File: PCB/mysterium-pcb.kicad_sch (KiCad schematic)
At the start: 221 parts, among them J1 AVR-ISP-6, J2 OLED, J3 TRRS1, J4 TRRS2, SW0 KEYSW, SW1 KEYSW, SW10 KEYSW, SW100 KEYSW, SW101 KEYSW, SW102 KEYSW, SW103 Rotary_Encoder_Switch, SW11 KEYSW, SW12 KEYSW, SW13 KEYSW, SW14 KEYSW, SW15 KEYSW, SW16 KEYSW, SW17 KEYSW, SW18 KEYSW, SW19 KEYSW, SW2 KEYSW, SW20 KEYSW, SW21 KEYSW, SW22 KEYSW, SW23 KEYSW, SW24 KEYSW, SW25 KEYSW, SW26 KEYSW, SW27 KEYSW, SW28 KEYSW, SW29 KEYSW, SW3 KEYSW, SW30 KEYSW, SW31 KEYSW, SW32 KEYSW, SW33 KEYSW, SW34 KEYSW, SW35 KEYSW, SW36 KEYSW, SW37 KEYSW, SW38 KEYSW, SW39 KEYSW, SW4 KEYSW, SW40 KEYSW, SW41 KEYSW, SW42 KEYSW, SW43 KEYSW, SW44 KEYSW, SW45 KEYSW, SW46 KEYSW, SW47 KEYSW, SW48 KEYSW, SW49 KEYSW, SW5 KEYSW, SW50 KEYSW, SW51 KEYSW, SW52 KEYSW, SW53 KEYSW, SW54 KEYSW, SW55 KEYSW, SW56 KEYSW, SW57 KEYSW, SW58 KEYSW, SW59 KEYSW, SW6 KEYSW, SW60 KEYSW, SW61 KEYSW, SW62 KEYSW, SW63 KEYSW, SW64 KEYSW, SW65 KEYSW, SW66 KEYSW, SW67 KEYSW, SW68 KEYSW, SW69 KEYSW, SW7 KEYSW, SW70 KEYSW, SW71 KEYSW, SW72 KEYSW, SW73 KEYSW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

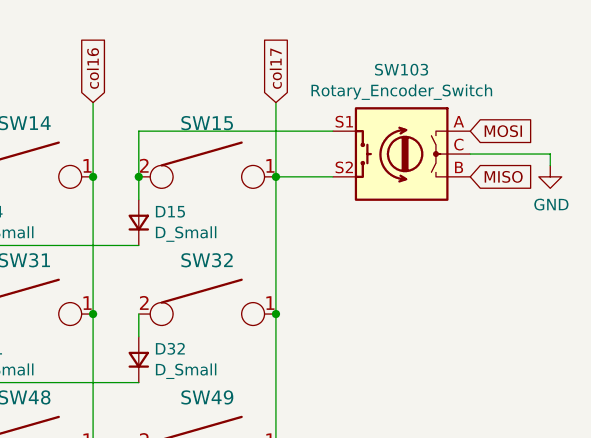
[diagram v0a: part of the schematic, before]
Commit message: Modifying PCB with hotswap keys
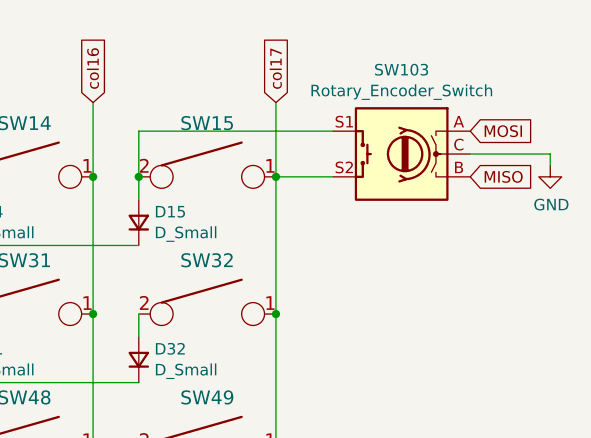
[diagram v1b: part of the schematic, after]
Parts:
- J3, J4: footprint kbd:MJ-4PP-9_1side -> My footprints:MJ-4PP-9_1side
- SW0, SW1, SW10, SW100, SW102, SW11, SW12, SW13, SW14, SW15, SW16, SW17, SW18, SW19, SW2, SW20, SW21, SW22, SW23, SW24, SW25, SW26, SW27, SW28, SW3, SW30, SW31, SW32, SW34, SW35, SW36, SW37, SW38, SW39, SW4, SW40, SW41, SW42, SW43, SW44, SW45, SW47, SW48, SW49, SW5, SW52, SW53, SW54, SW55, SW56, SW57, SW58, SW59, SW6, SW60, SW61, SW62, SW65, SW66, SW67, SW68, SW69, SW7, SW70, SW71, SW72, SW73, SW74, SW76, SW8, SW80, SW83, SW84, SW89, SW9, SW92, SW93, SW94, SW96, SW98, SW99: footprint cftkb:SW_Cherry_MX1A_1.00u_PCB-NOSCREEN -> acheron_MXH_MetalRings:MX100H
- SW101, SW50: footprint cftkb:SW_Cherry_MX1A_1.75u_PCBNOSCREEN -> acheron_MXH_MetalRings:MX175H
- SW103: footprint cftkb:RotaryEncoder_Alps_EC11E-Switch_Vertical_H20mm-for-MX -> My footprints:RotaryEncoder_Alps_EC11E-Switch_Vertical_H20mm-for-MX
- SW29: footprint cftkb:SW_Cherry_MX1A_2.00u_PCBNOSCREEN -> acheron_MXH_MetalRings:MX200H
- SW33, SW46, SW77, SW81, SW86, SW90: footprint cftkb:SW_Cherry_MX1A_1.50u_PCBNOSCREEN -> acheron_MXH_MetalRings:MX150H
- SW51, SW78, SW79, SW82, SW85, SW87, SW88, SW91, SW97: footprint cftkb:SW_Cherry_MX1A_1.25u_PCBNOSCREEN -> acheron_MXH_MetalRings:MX125H
- SW63, SW64: footprint cftkb:SW_Cherry_MX1A_2.25u_PCBNOSCREEN -> acheron_MXH_MetalRings:MX225H
- SW75: footprint cftkb:SW_Cherry_MX1A_2.75u_PCB_NOSCREEN -> acheron_MXH_MetalRings:MX275H
- SW95: footprint cftkb:SW_Cherry_MX1A_ISOEnter_PCB_ReversedStabilizer -> acheron_MXH_MetalRings:MX_ISOEnterH
